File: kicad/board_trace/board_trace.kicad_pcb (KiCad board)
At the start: 2 copper layers, 40.7 x 62.4 mm, 62 parts, among them J1 USB3 stacked Type-A (candidat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, J2 USB3 stacked Type-A (candidat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, J3 SFP20 (candidate), J4 DC barrel jack (unidentified), U1 VL813 (candidate), U2 UNKNOWN, Y1 25MHz

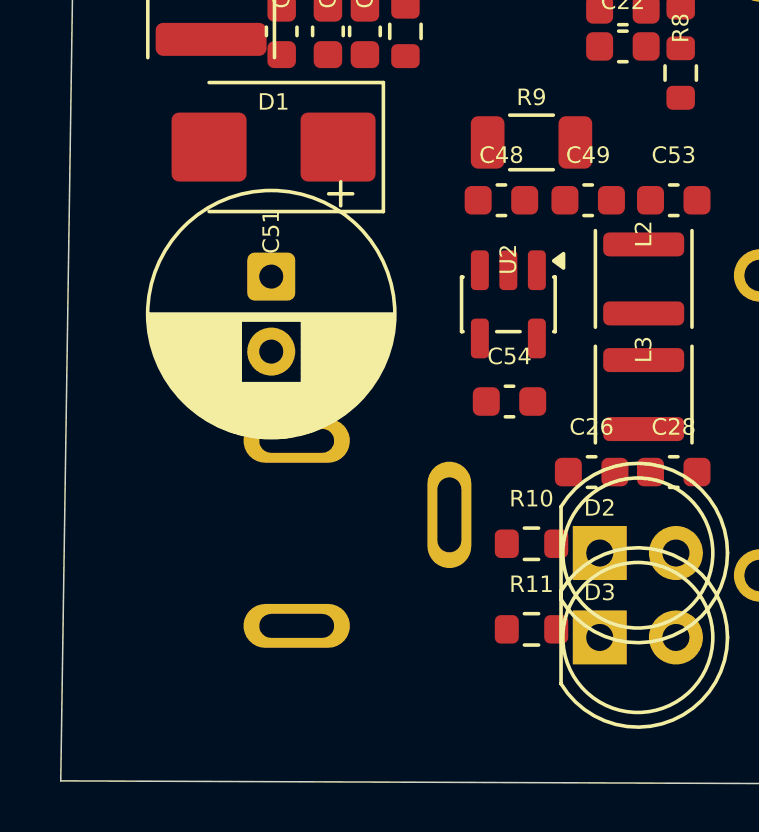
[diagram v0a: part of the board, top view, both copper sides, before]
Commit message: board_trace: place XKB DC-005-2.5A-2.0 DC jack as J4; downsize C51
Replace the provisional BarrelJack_PhotoTrace proxy with the real XKB
DC-005-2.5A-2.0 panel-mount DC power jack (LCSC C319099). The footprint is
transcribed from the vendor datasheet "PCB HOLES (TOP VIEW)" drawing and the
EasyEDA package: three 3.0x0.8mm slots, the two collinear terminals 6.10mm apart
and the break terminal 4.60mm to the side. Pin numbers follow the datasheet
SCHEDULE (1 tip/centre, 2 break/switch, 3 outer/sleeve). J4 is placed on the two
photo-measured collinear holes with the barrel facing the board edge; its break
terminal lands within ~0.65mm of the old proxy's third joint.

Downsize C51 from a D8.0mm to a D5.0mm radial can: the real jack body is longer
than the photo proxy and would encroach on an 8mm capacitor. Both stock footprints
share the 2.50mm lead pitch, so the leads stay in the same photo-measured holes.
Capacitance and height remain unmeasured.

- Add the already-fitted CAGE1 (CND-tek C5441174) and the real J4/C51 to
  scripts/04_review_plan.py + placement_plan.json; 06_check_saved.py passes again
  at 62 parts (the cage commit had left the plan/check stale).
- Native DRC 322 -> 283 (128 errors, 155 warnings), 0 unconnected, no tracks or
  named nets: the smaller C51 silkscreen removes 37 silk warnings, plus one
  courtyard overlap and one PTH-inside-courtyard finding. J4/C51 courtyards clear
  by 0.37mm.
- pcbnew re-serialises PTH pads without the explicit "*.Mask" wildcard (KiCad
  re-derives it from the project on load), so the cage's 17 pads are normalised;
  no functional change.
- New scripts/07_place_dc_jack.py (in-place edit, keeps UUIDs/order) and
  libs/lcsc.pretty/C319099_DC-005-2.5A-2.0.kicad_mod.

Placement evidence only; no hub electrical change. Hub J7 remains "input TBD".
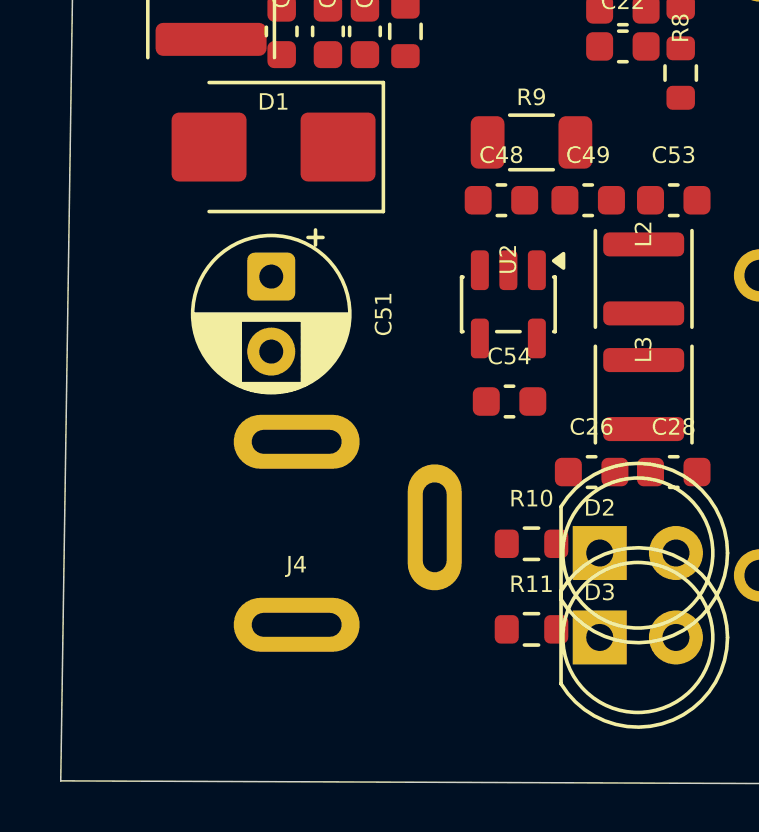
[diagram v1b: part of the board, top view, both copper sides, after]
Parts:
- C51: footprint Capacitor_THT:CP_Radial_D8.0mm_P2.50mm -> Capacitor_THT:CP_Radial_D5.0mm_P2.50mm
- J4: value DC barrel jack (unidentified) -> DC-005-2.5A-2.0; footprint trace:BarrelJack_PhotoTrace -> lcsc:C319099_DC-005-2.5A-2.0
- moved J4 6.13 mm to (135.9, 131.5)
